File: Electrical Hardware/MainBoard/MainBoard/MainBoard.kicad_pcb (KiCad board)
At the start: 2 copper layers, 49.4 x 51.7 mm, 79 parts, among them J1 SM02B-SRSS-TB_LFSN_, J10 UJC-HP-M-G-5-MSMT-TR, J11 USB4500-03-0-A_REVA1, J2 Conn_01x04_Socket, J3 Conn_01x04_Socket, J4 Conn_01x04_Socket, J5 USB_B_Micro, J6 Thermistor, J7 62684-401100ALF, J8 Conn_01x02_Socket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

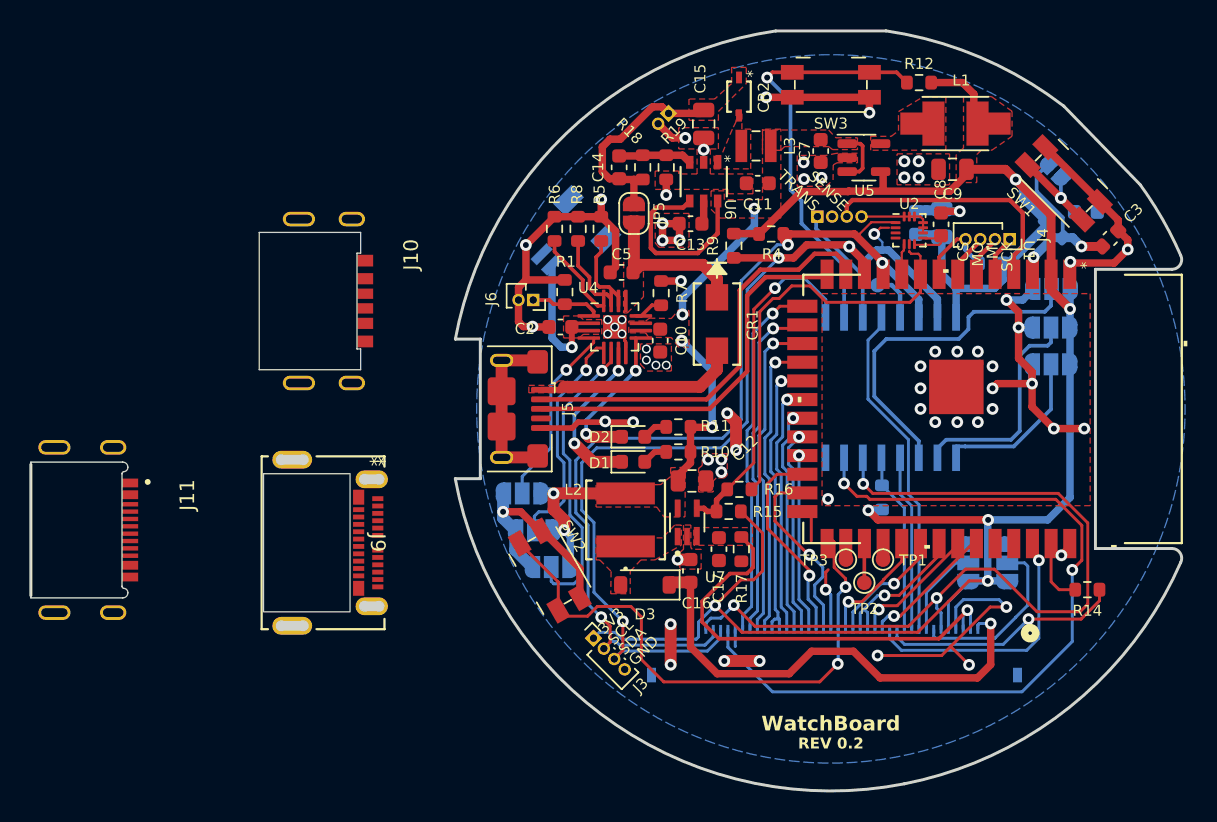
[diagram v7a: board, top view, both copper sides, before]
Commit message: Settle USB-C schematic update; begin USB-C layout edits
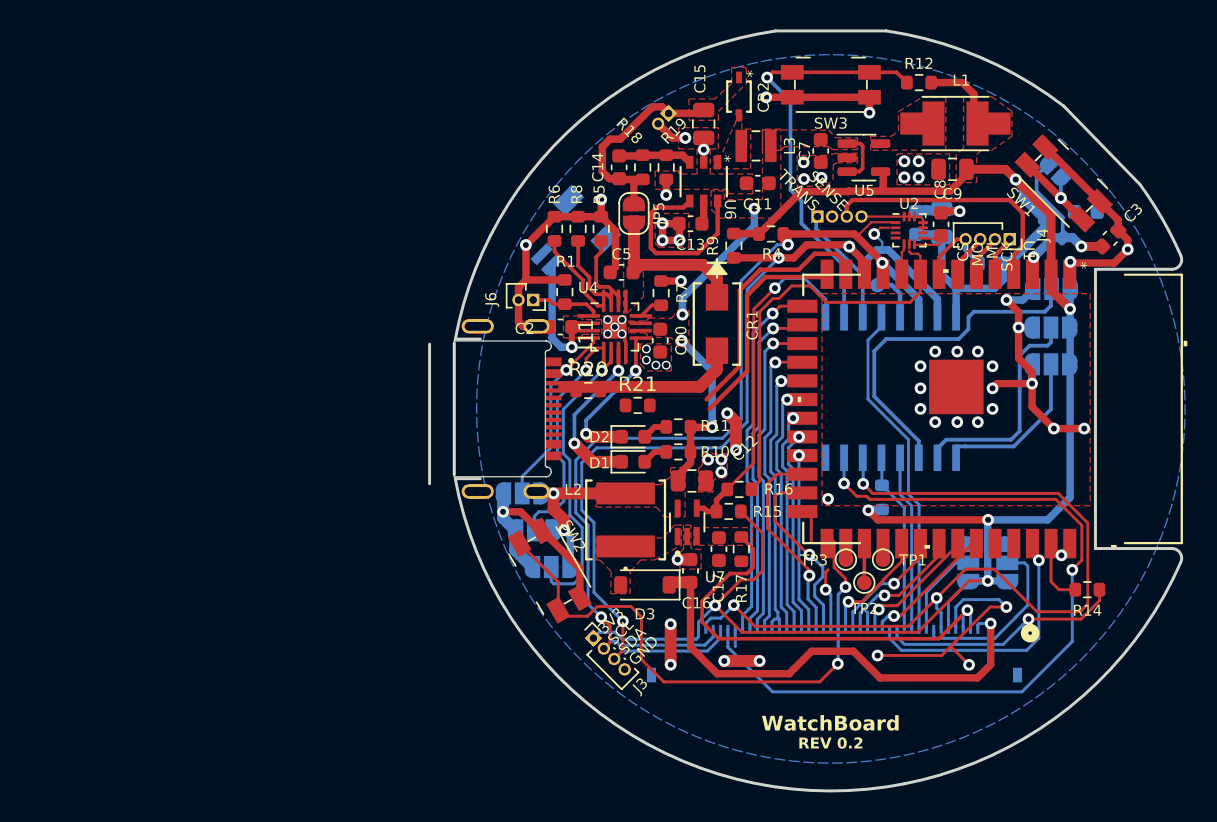
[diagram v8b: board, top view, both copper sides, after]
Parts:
- removed J10: UJC-HP-M-G-5-MSMT-TR, UJC_HP_M_G_5_MSMT_TR:CUI_UJC-HP-M-G-5-MSMT-TR
- removed J5: USB_B_Micro, Connector_USB:USB_Micro-B_Amphenol_10118193-0001LF_Horizontal
- removed J9: 1054550101, 1054550101:105455-0101_MOL
- added R20: 5.1K, Resistor_SMD:R_0603_1608Metric, F.Cu at (77.2, 49.7)
- added R21: 5.1K, Resistor_SMD:R_0603_1608Metric, F.Cu at (80.6, 50.7)
- moved J11 30.0 mm to (69.7, 50.9)
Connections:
- CR1 pad 2: Net-(J5-VBUS) -> Net-(J11-VBUS_A)
- J11 pad A1_B12: unconnected-(J11-GND_A-PadA1_B12) -> GND
- J11 pad A4_B9: unconnected-(J11-VBUS_A-PadA4_B9) -> Net-(J11-VBUS_A)
- J11 pad A5: unconnected-(J11-CC1-PadA5) -> Net-(J11-CC1)
- J11 pad A6: unconnected-(J11-DP1-PadA6) -> D+
- J11 pad A7: unconnected-(J11-DN1-PadA7) -> D-
- J11 pad B1_A12: unconnected-(J11-GND_B-PadB1_A12) -> GND
- J11 pad B4_A9: unconnected-(J11-VBUS_B-PadB4_A9) -> Net-(J11-VBUS_A)
- J11 pad B5: unconnected-(J11-CC2-PadB5) -> Net-(J11-CC2)
- J11 pad B6: unconnected-(J11-DP2-PadB6) -> D+
- J11 pad B7: unconnected-(J11-DN2-PadB7) -> D-
- J11 pad SH1: unconnected-(J11-SHELL_GND-PadSH1) -> GND
- J11 pad SH2: unconnected-(J11-SHELL_GND__1-PadSH2) -> GND
- J11 pad SH3: unconnected-(J11-SHELL_GND__2-PadSH3) -> GND
- J11 pad SH4: unconnected-(J11-SHELL_GND__3-PadSH4) -> GND
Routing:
- net GND: track 153.3 -> 135.2 mm, vias 66 -> 64
- net Net-(J5-VBUS): track 13.8 -> 0.00 mm
- net Net-(J11-VBUS_A): track 0.00 -> 12.5 mm
- net D+: track 26.3 -> 14.8 mm
- net D-: track 29.8 -> 18.6 mm
- removed copper zone on F.Cu, net (none)
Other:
- board size 49.4 x 51.7 mm -> 51.2 x 51.7 mm
